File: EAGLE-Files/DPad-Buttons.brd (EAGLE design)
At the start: 49.5 x 31.8 mm, 1 part

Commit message: Updated board layouts
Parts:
- added JP2, JP3, JP4: (no value), pinhead:1X01
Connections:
- net GND: now also JP2.1, JP3.1, JP4.1
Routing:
- net BUT4: track 86.6 -> 84.2 mm
- net BUT3: track 64.7 -> 62.5 mm
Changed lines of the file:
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@@
 <hole x="48.26" y="16.51" drill="0.35"/>
 <hole x="19.05" y="16.51" drill="0.35"/>
+<dimension x1="19.05" y1="16.51" x2="27.94" y2="25.4" x3="16.509996875" y3="27.94" textsize="1.778" layer="1"/>
+<dimension x1="19.05" y1="16.51" x2="10.16" y2="7.62" x3="6.985" y3="19.685" textsize="1.778" layer="1" dtype="diameter"/>
+<hole x="27.94" y="25.4" drill="0.35"/>
+<hole x="10.16" y="7.62" drill="0.35"/>
 </plain>
 <attributes>
@@
 <attribute name="VALUE" x="46.99" y="15.875" size="1.27" layer="27"/>
 </element>
+<element name="JP2" library="pinhead" library_urn="urn:adsk.eagle:library:325" package="1X01" package3d_urn="urn:adsk.eagle:package:22485/2" value="" x="41.91" y="29.21" smashed="yes">
+<attribute name="NAME" x="40.5638" y="31.0388" size="1.27" layer="25" ratio="10"/>
+<attribute name="POPULARITY" value="64" x="41.91" y="29.21" size="1.778" layer="27" display="off"/>
+<attribute name="VALUE" x="40.64" y="26.035" size="1.27" layer="27"/>
+</element>
+<element name="JP3" library="pinhead" library_urn="urn:adsk.eagle:library:325" package="1X01" package3d_urn="urn:adsk.eagle:package:22485/2" value="" x="34.29" y="29.21" smashed="yes">
+<attribute name="NAME" x="32.9438" y="31.0388" size="1.27" layer="25" ratio="10"/>
+<attribute name="POPULARITY" value="64" x="34.29" y="29.21" size="1.778" layer="27" display="off"/>
+<attribute name="VALUE" x="33.02" y="26.035" size="1.27" layer="27"/>
+</element>
+<element name="JP4" library="pinhead" library_urn="urn:adsk.eagle:library:325" package="1X01" package3d_urn="urn:adsk.eagle:package:22485/2" value="" x="38.1" y="29.21" smashed="yes">
+<attribute name="NAME" x="36.7538" y="31.0388" size="1.27" layer="25" ratio="10"/>
+<attribute name="POPULARITY" value="64" x="38.1" y="29.21" size="1.778" layer="27" display="off"/>
+<attribute name="VALUE" x="36.83" y="26.035" size="1.27" layer="27"/>
+</element>
 </elements>
 <signals>
@@
 <vertex x="54.61" y="36.83"/>
 </polygon>
+<contactref element="JP2" pad="1"/>
+<contactref element="JP3" pad="1"/>
+<contactref element="JP4" pad="1"/>
 </signal>
 <signal name="BUT1">
@@
 <wire x1="15.113" y1="25.273" x2="15.113" y2="28.702" width="0.1524" layer="16"/>
 <wire x1="15.113" y1="28.702" x2="22.606" y2="28.702" width="0.1524" layer="16"/>
-<wire x1="46.99" y1="26.67" x2="45.72" y2="26.67" width="0.635" layer="16"/>
-<wire x1="45.72" y1="26.67" x2="44.1833" y2="28.2067" width="0.635" layer="16"/>
-<wire x1="44.1833" y1="28.2067" x2="22.606" y2="28.2067" width="0.635" layer="16"/>
+<wire x1="46.99" y1="26.67" x2="30.48" y2="26.67" width="0.635" layer="16"/>
+<wire x1="30.48" y1="26.67" x2="28.9433" y2="28.2067" width="0.635" layer="16"/>
+<wire x1="28.9433" y1="28.2067" x2="22.606" y2="28.2067" width="0.635" layer="16"/>
 </signal>
 <signal name="BUT2">
@@
 <wire x1="46.99" y1="21.59" x2="45.72" y2="21.59" width="0.635" layer="16"/>
 <wire x1="45.72" y1="21.59" x2="44.45" y2="20.32" width="0.635" layer="16"/>
-<wire x1="44.45" y1="20.32" x2="36.83" y2="20.32" width="0.635" layer="16"/>
-<wire x1="36.83" y1="20.32" x2="33.02" y2="16.51" width="0.635" layer="16"/>
-<wire x1="33.02" y1="16.51" x2="33.02" y2="12.7" width="0.635" layer="16"/>
-<wire x1="26.67" y1="6.35" x2="22.606" y2="6.35" width="0.635" layer="16"/>
-<wire x1="33.02" y1="12.7" x2="26.67" y2="6.35" width="0.635" layer="16"/>
+<wire x1="44.45" y1="20.32" x2="41.529" y2="20.32" width="0.635" layer="16"/>
+<wire x1="41.529" y1="20.32" x2="27.559" y2="6.35" width="0.635" layer="16"/>
+<wire x1="27.559" y1="6.35" x2="22.606" y2="6.35" width="0.635" layer="16"/>
 </signal>
 <signal name="BUT4">
@@
 <wire x1="8.89" y1="12.954" x2="7.366" y2="12.954" width="0.1524" layer="16"/>
 <wire x1="7.366" y1="12.954" x2="7.366" y2="20.447" width="0.1524" layer="16"/>
-<wire x1="13.97" y1="2.54" x2="8.89" y2="7.62" width="0.635" layer="16"/>
-<wire x1="8.89" y1="7.62" x2="8.89" y2="12.954" width="0.635" layer="16"/>
-<wire x1="46.99" y1="19.05" x2="37.719" y2="19.05" width="0.635" layer="16"/>
-<wire x1="37.719" y1="19.05" x2="34.29" y2="15.621" width="0.635" layer="16"/>
-<wire x1="34.29" y1="11.43" x2="25.4" y2="2.54" width="0.635" layer="16"/>
+<wire x1="46.99" y1="19.05" x2="41.91" y2="19.05" width="0.635" layer="16"/>
+<wire x1="41.91" y1="19.05" x2="25.4" y2="2.54" width="0.635" layer="16"/>
 <wire x1="25.4" y1="2.54" x2="13.97" y2="2.54" width="0.635" layer="16"/>
-<wire x1="34.29" y1="15.621" x2="34.29" y2="11.43" width="0.635" layer="16"/>
+<wire x1="13.97" y1="2.54" x2="12.7" y2="3.81" width="0.635" layer="16"/>
+<wire x1="12.7" y1="9.144" x2="8.89" y2="12.954" width="0.635" layer="16"/>
+<wire x1="12.7" y1="3.81" x2="12.7" y2="9.144" width="0.635" layer="16"/>
 </signal>
 <signal name="EBUT1">

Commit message: Updated boards and models
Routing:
- net BUT1: track 56.8 -> 57.9 mm
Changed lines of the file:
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@@
 <hole x="46.99" y="16.51" drill="0.35"/>
 <hole x="48.26" y="16.51" drill="0.35"/>
-<hole x="19.05" y="16.51" drill="0.35"/>
-<dimension x1="19.05" y1="16.51" x2="27.94" y2="25.4" x3="16.509996875" y3="27.94" textsize="1.778" layer="1"/>
-<dimension x1="19.05" y1="16.51" x2="10.16" y2="7.62" x3="6.985" y3="19.685" textsize="1.778" layer="1" dtype="diameter"/>
-<hole x="27.94" y="25.4" drill="0.35"/>
-<hole x="10.16" y="7.62" drill="0.35"/>
+<dimension x1="19.05" y1="16.51" x2="30.48" y2="27.94" x3="17.78" y3="29.21" textsize="1.778" layer="1"/>
+<dimension x1="19.05" y1="16.51" x2="7.62" y2="5.08" x3="5.714996875" y3="18.415" textsize="1.778" layer="1" dtype="diameter"/>
+<hole x="30.48" y="27.94" drill="0.35"/>
+<hole x="7.62" y="5.08" drill="0.35"/>
 </plain>
 <attributes>
@@
 <wire x1="15.113" y1="25.273" x2="15.113" y2="28.702" width="0.1524" layer="16"/>
 <wire x1="15.113" y1="28.702" x2="22.606" y2="28.702" width="0.1524" layer="16"/>
-<wire x1="46.99" y1="26.67" x2="30.48" y2="26.67" width="0.635" layer="16"/>
-<wire x1="30.48" y1="26.67" x2="28.9433" y2="28.2067" width="0.635" layer="16"/>
-<wire x1="28.9433" y1="28.2067" x2="22.606" y2="28.2067" width="0.635" layer="16"/>
+<wire x1="46.99" y1="26.67" x2="45.72" y2="26.67" width="0.635" layer="16"/>
+<wire x1="45.72" y1="26.67" x2="44.45" y2="25.4" width="0.635" layer="16"/>
+<wire x1="44.45" y1="25.4" x2="27.94" y2="25.4" width="0.635" layer="16"/>
+<wire x1="27.94" y1="25.4" x2="25.1333" y2="28.2067" width="0.635" layer="16"/>
+<wire x1="25.1333" y1="28.2067" x2="22.606" y2="28.2067" width="0.635" layer="16"/>
 </signal>
 <signal name="BUT2">

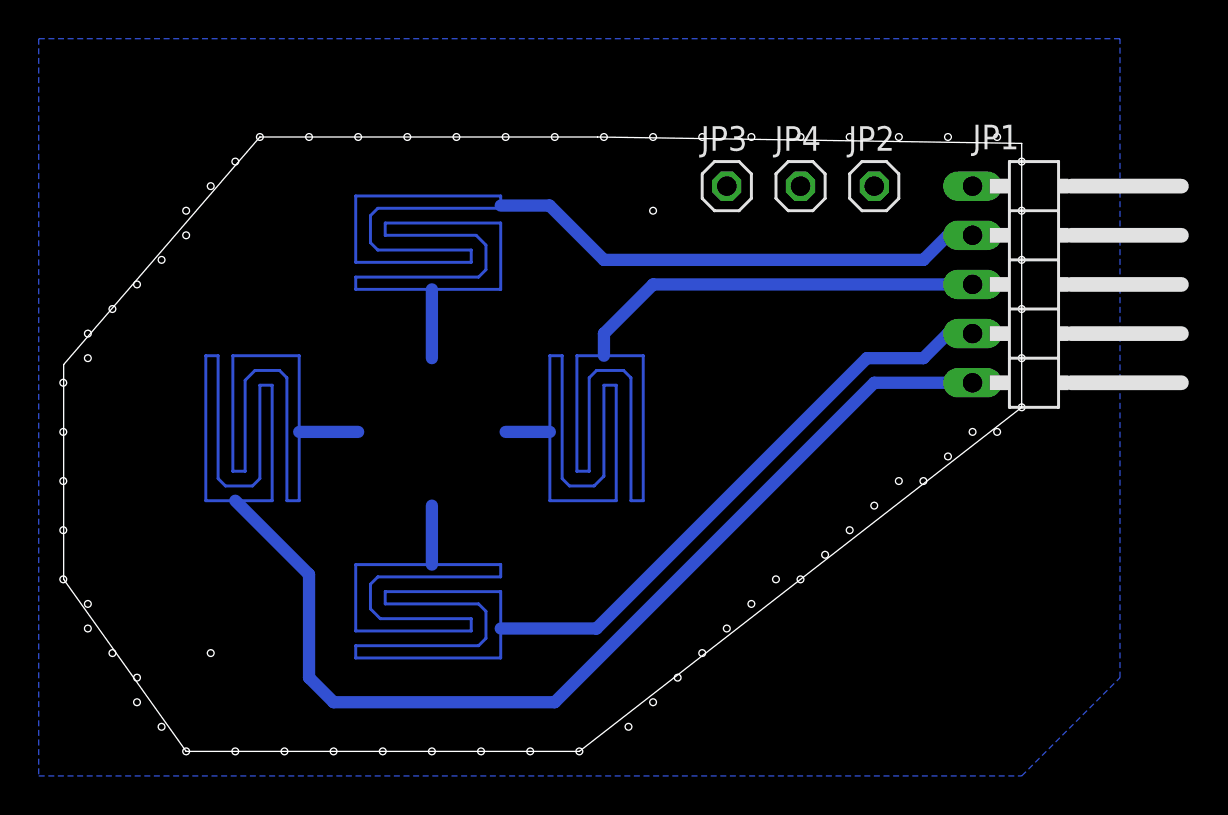
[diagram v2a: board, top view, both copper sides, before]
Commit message: Updated the DPad and Four Buttons PCB designs for production
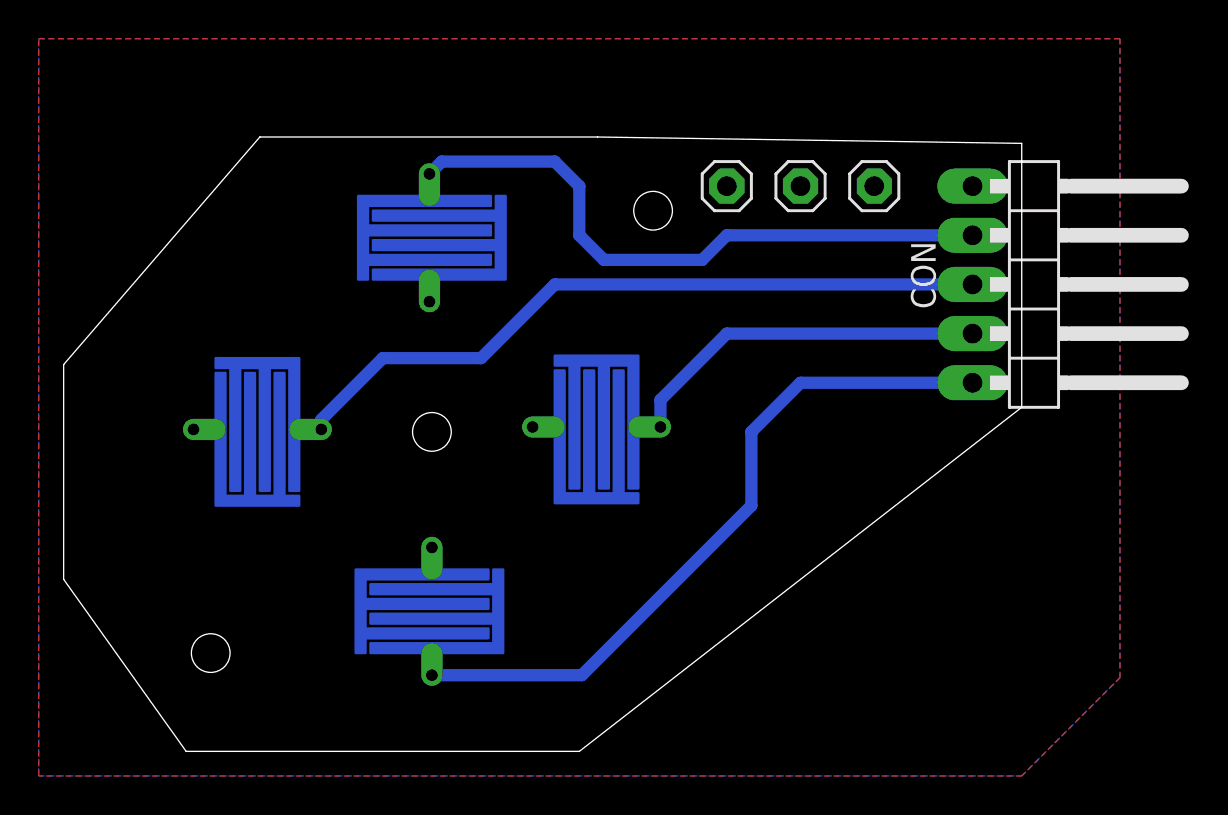
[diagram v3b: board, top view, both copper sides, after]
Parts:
- added BTN1, BTN2, BTN3, BTN4: BTN_5MM_LONG, surfacebuttons:BTN_5MM_LONG
- renumbered JP1 to CON, JP2 to GND_3, JP3 to GND_2, JP4 to GND_1
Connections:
- removed net BUT1: CON.2
- removed net BUT2: CON.3
- removed net BUT3: CON.4
- removed net BUT4: CON.5
- new net N$1: BTN1.P$1, CON.2
- new net N$2: BTN4.P$1, CON.5
- new net N$3: BTN3.P$1, CON.4
- new net N$4: BTN2.P$1, CON.3
- net GND: now also BTN1.P$2, BTN2.P$2, BTN3.P$2, BTN4.P$2
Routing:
- net BUT4: track 84.2 -> 0.00 mm
- net BUT3: track 62.5 -> 0.00 mm
- net BUT1: track 57.9 -> 0.00 mm
- net BUT2: track 53.1 -> 0.00 mm
- net N$4: track 0.00 -> 37.1 mm
- net N$2: track 0.00 -> 36.4 mm
- net EBUT1: track 35.3 -> 0.00 mm
- net EBUT3: track 34.8 -> 0.00 mm
- net EBUT4: track 34.8 -> 0.00 mm
- net EBUT2: track 34.0 -> 0.00 mm
- net N$1: track 0.00 -> 32.4 mm
- net N$3: track 0.00 -> 18.9 mm
- added copper zone on layer 1, net GND
- removed copper zone on layer 16, net BUT1
- removed copper zone on layer 16, net BUT2
- removed copper zone on layer 16, net BUT3
- removed copper zone on layer 16, net BUT4
- removed copper zone on layer 16, net EBUT1
- removed copper zone on layer 16, net EBUT2
- removed copper zone on layer 16, net EBUT3
- removed copper zone on layer 16, net EBUT4
